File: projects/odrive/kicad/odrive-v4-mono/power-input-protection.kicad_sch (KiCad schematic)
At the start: 19 parts, among them J1 PC 16/2-ST, Q1 NVMFS5C628NL | BSC027N10NS5

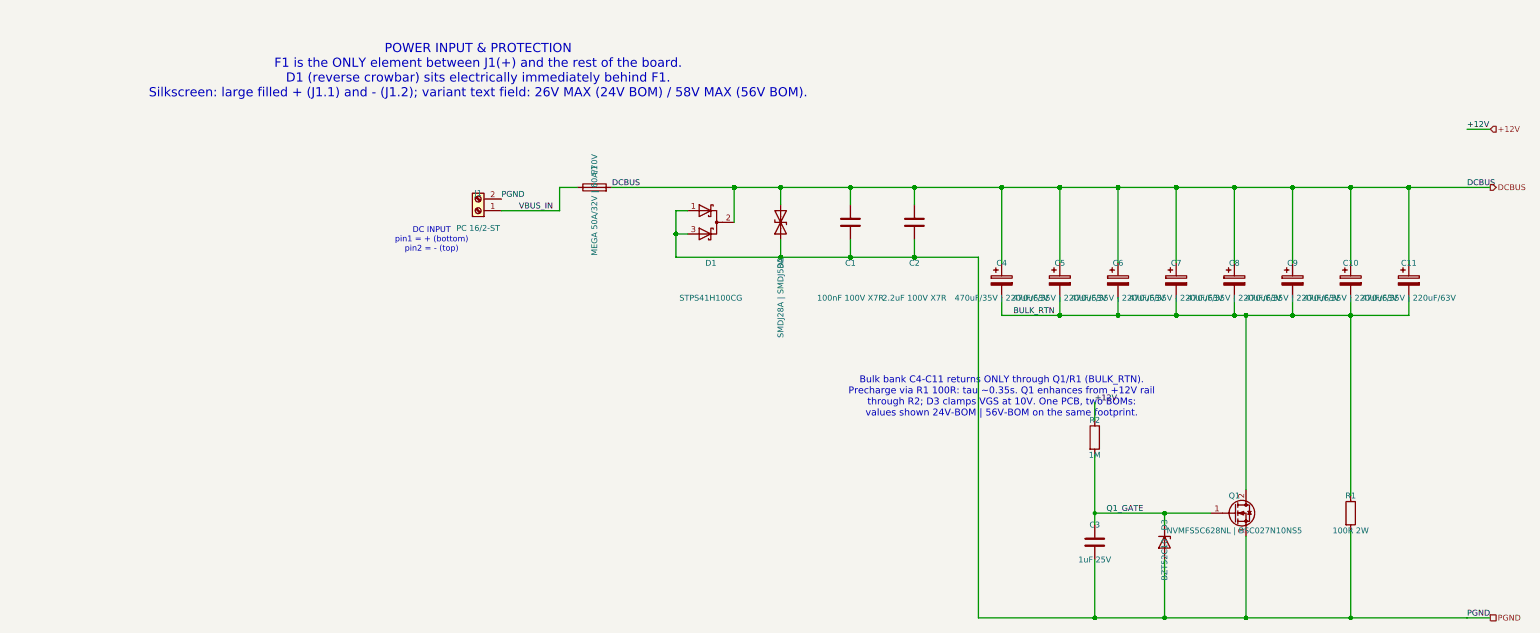
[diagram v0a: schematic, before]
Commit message: Checkpoint ODrive 56 V recovery and modular handoff
Preserve corrected schematics, local libraries, partial PCB routing, firmware diagnostics, analysis tools and the independent modular-study handoff. The board remains incomplete with 381 unconnected items and 415 DRC warnings.

Validation: 52 host tests, ARM component compilation, schematic/PCB parity, native copper preservation, DRC, STEP export, Python lint, shellcheck and nix fmt. Known Konnect-generated schematic whitespace is retained. No fabrication or hardware validation is claimed.
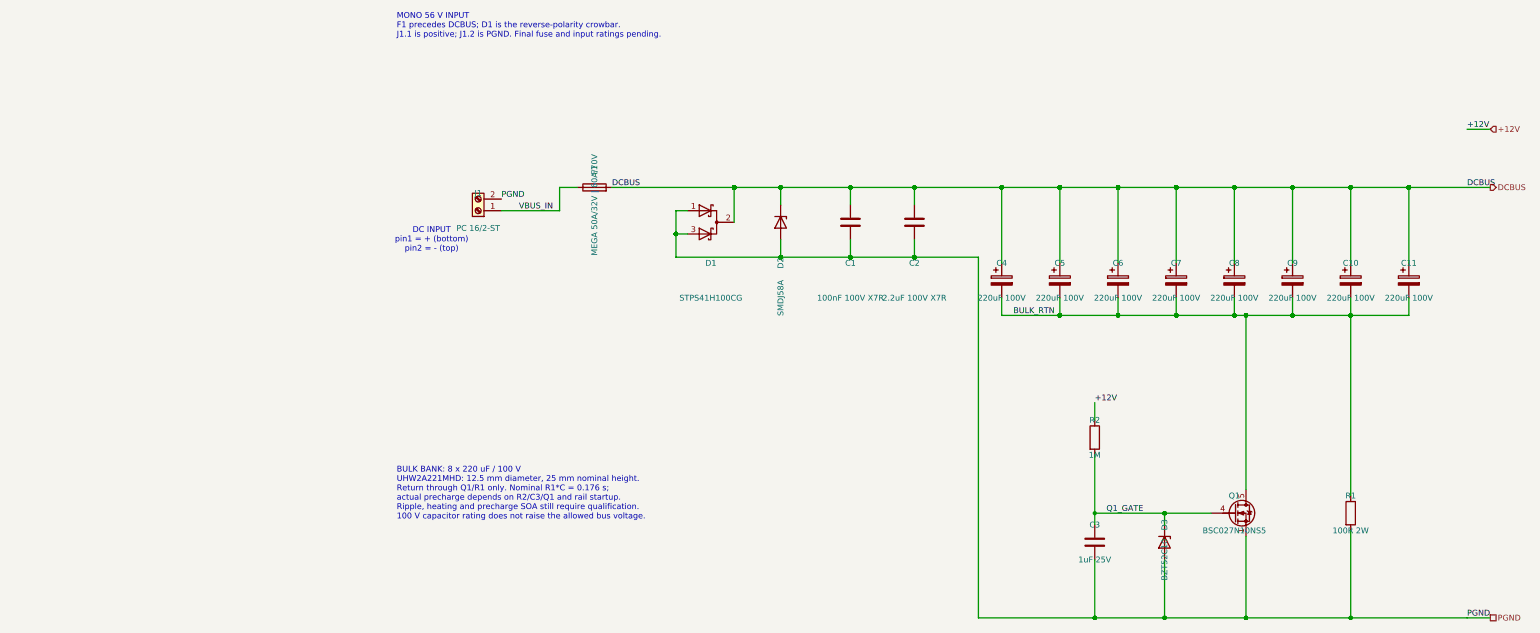
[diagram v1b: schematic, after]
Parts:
- C10, C11, C4, C5, C6, C7, C8, C9: value 470uF/35V | 220uF/63V -> 220uF 100V; footprint Capacitor_THT:CP_Radial_D10.0mm_P5.00mm -> Capacitor_THT:CP_Radial_D12.5mm_P5.00mm; Design_note (none) -> 12.5 mm diameter x 25 mm nominal height, 5 mm lead pitch. B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; MPN (none) -> UHW2A221MHD; MPN_24V Panasonic EEU-FR1V471 (470uF/35V) -> (none); MPN_56V Panasonic EEU-FR1J221 (220uF/63V) -> UHW2A221MHD; Manufacturer (none) -> Nichicon; Tolerance (none) -> 20%; Voltage (none) -> 100 V
- D2: value SMDJ28A | SMDJ58A -> SMDJ58A; symbol Device:D_TVS -> Device:D_Zener; Design_note (none) -> Unidirectional TVS: cathode pad 1 to DCBUS, anode pad 2 to 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; MPN (none) -> SMDJ58A; Manufacturer (none) -> Littelfuse
- Q1: value NVMFS5C628NL | BSC027N10NS5 -> BSC027N10NS5; footprint Package_SO:PowerPAK_SO-8_Single -> odrive-mono:Infineon_PG-TSON-8-3; symbol Transistor_FET:Q_NMOS_GDS -> Transistor_FET:Q_NMOS_SSSGD_AvalancheRated; Design_note (none) -> 100V selection; verify losses, SOA, cooling and mask apertu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; MPN (none) -> BSC027N10NS5ATMA1; MPN_24V onsemi NVMFS5C628NL (60V) -> (none); MPN_56V Infineon BSC027N10NS5 (100V) -> BSC027N10NS5ATMA1; Manufacturer (none) -> Infineon
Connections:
- net BULK_RTN: now also Q1.5 (D); no longer Q1.2 (D)
- net DCBUS: now also D2.1 (K); no longer D2.2 (A2)
- net PGND: now also D2.2 (A), Q1.1 (S), Q1.2 (S); no longer D2.1 (A1)
- net Q1_GATE: now also Q1.4 (G); no longer Q1.1 (G)
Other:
- note added: "BULK BANK: 8 x 220 uF / 100 V UHW2A221MHD: 12.5 mm diameter, 25 mm nominal height. Return through Q1/R1 only. Nominal R1*C = 0.176 s; actual precharge depends on R2/C3/Q1 and rail startup. Ripple, heating and precharge SOA still require qualification. 100 V capacitor rating does not raise the allowed bus voltage."
- note added: "MONO 56 V INPUT F1 precedes DCBUS; D1 is the reverse-polarity crowbar. J1.1 is positive; J1.2 is PGND. Final fuse and input ratings pending."
- note removed: "Bulk bank C4-C11 returns ONLY through Q1/R1 (BULK_RTN). Precharge via R1 100R: tau ~0.35s. Q1 enhances from +12V rail through R2; D3 clamps VGS at 10V. One PCB, two BOMs: values shown 24V-BOM | 56V-BOM on the same footprint."
- note removed: "POWER INPUT & PROTECTION F1 is the ONLY element between J1(+) and the rest of the board. D1 (reverse crowbar) sits electrically immediately behind F1. Silkscreen: large filled + (J1.1) and - (J1.2); variant text field: 26V MAX (24V BOM) / 58V MAX (56V BOM)."
- moved on the sheet: D2
